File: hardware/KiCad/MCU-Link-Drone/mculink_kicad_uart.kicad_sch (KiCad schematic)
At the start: 11 parts, among them J7 1x3pos, 100mil pitch, U10 SN74LVC1T45GW, U9 SN74LVC1T45GW

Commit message: updated with drone project files
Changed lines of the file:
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@@
 	(text "UART Interface to Target"
 		(exclude_from_sim no)
-		(at 158.75 21.59 0)
+		(at 167.64 21.59 0)
 		(effects
 			(font

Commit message: worked on layout
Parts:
- J7: footprint Connector_PinHeader_2.54mm:PinHeader_1x03_P2.54mm_Horizontal -> Connector_PinHeader_2.54mm:PinHeader_1x03_P2.54mm_Vertical
- U10, U9: footprint Package_TO_SOT_SMD:SOT-23-6 -> Package_TO_SOT_SMD:SOT-363_SC-70-6
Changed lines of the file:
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@@
 			)
 		)
-		(property "Footprint" "Package_TO_SOT_SMD:SOT-23-6"
+		(property "Footprint" "Package_TO_SOT_SMD:SOT-363_SC-70-6"
 			(at 76.2 85.09 0)
 			(effects
@@
 			)
 		)
-		(property "Footprint" "Package_TO_SOT_SMD:SOT-23-6"
+		(property "Footprint" "Package_TO_SOT_SMD:SOT-363_SC-70-6"
 			(at 76.2 123.19 0)
 			(effects
@@
 			)
 		)
-		(property "Footprint" "Connector_PinHeader_2.54mm:PinHeader_1x03_P2.54mm_Horizontal"
+		(property "Footprint" "Connector_PinHeader_2.54mm:PinHeader_1x03_P2.54mm_Vertical"
 			(at 140.97 76.2 0)
 			(effects

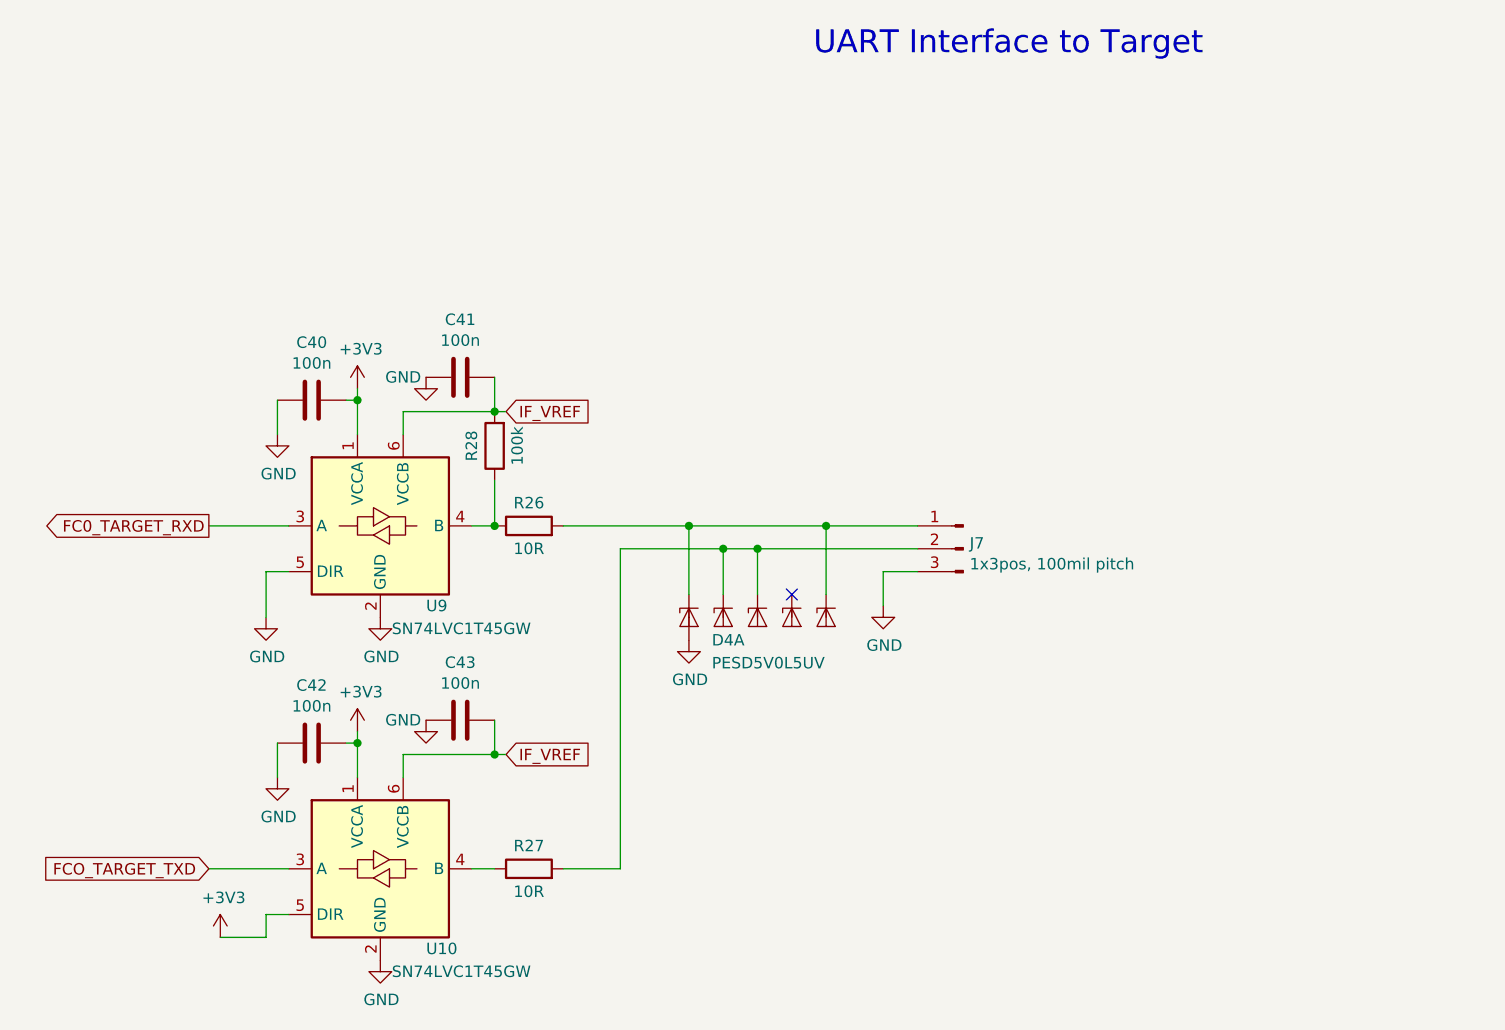
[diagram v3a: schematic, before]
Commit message: added JST-GH for UART
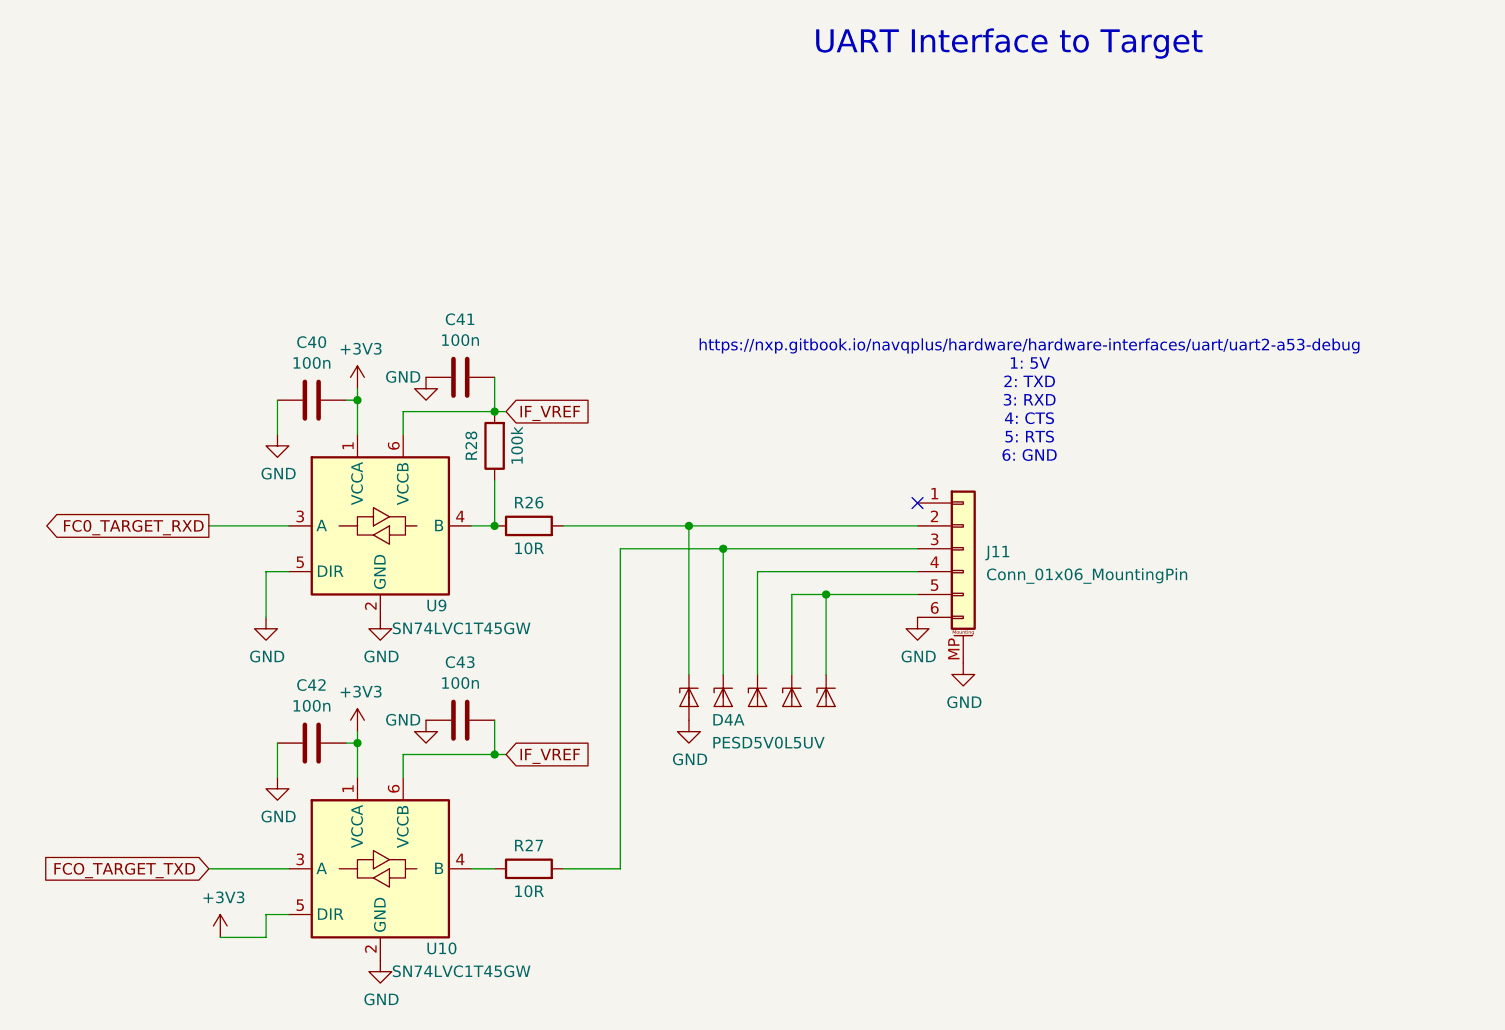
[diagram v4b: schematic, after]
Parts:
- removed J7: 1x3pos, 100mil pitch, Connector_PinHeader_2.54mm:PinHeader_1x03_P2.54mm_Vertical, symbol mculink_kicad-rescue:Conn_01x03_Male-Connector
- added J11: Conn_01x06_MountingPin, Connector_JST:JST_GH_BM06B-GHS-TBT_1x06-1MP_P1.25mm_Vertical, symbol Connector_Generic_MountingPin:Conn_01x06_MountingPin
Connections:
- net GND: now also J11.6 (Pin_6), J11.MP (MountPin)
- net at D4.1 (K1), R26.2: now also J11.2 (Pin_2); no longer D4.6 (K5)
- net at D4.3 (K2), R27.2: now also J11.3 (Pin_3); no longer D4.4 (K3)
- net at D4.5 (K4): now also D4.6 (K5), J11.5 (Pin_5)
- new net: D4.4 (K3), J11.4 (Pin_4)
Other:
- note added: "https://nxp.gitbook.io/navqplus/hardware/hardware-interfaces/uart/uart2-a53-debug 1: 5V 2: TXD 3: RXD 4: CTS 5: RTS 6: GND"
- moved on the sheet: D4A

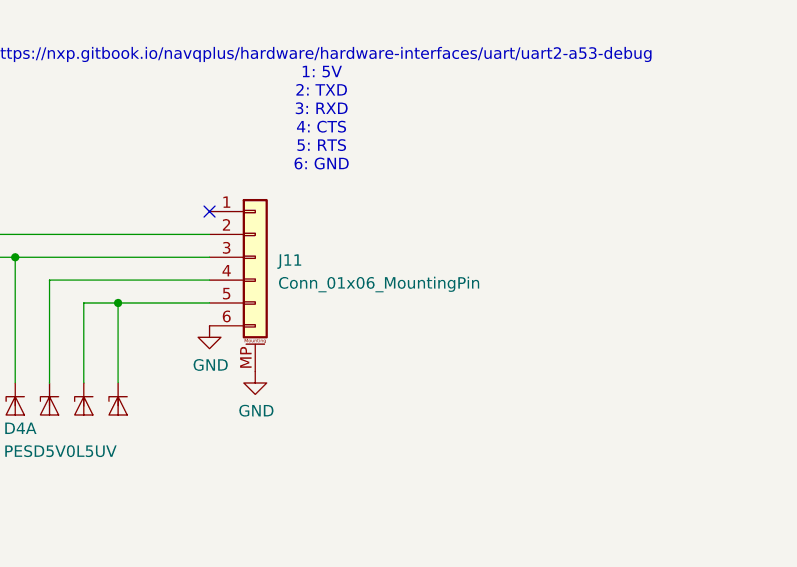
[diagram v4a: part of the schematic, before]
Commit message: updated schematics
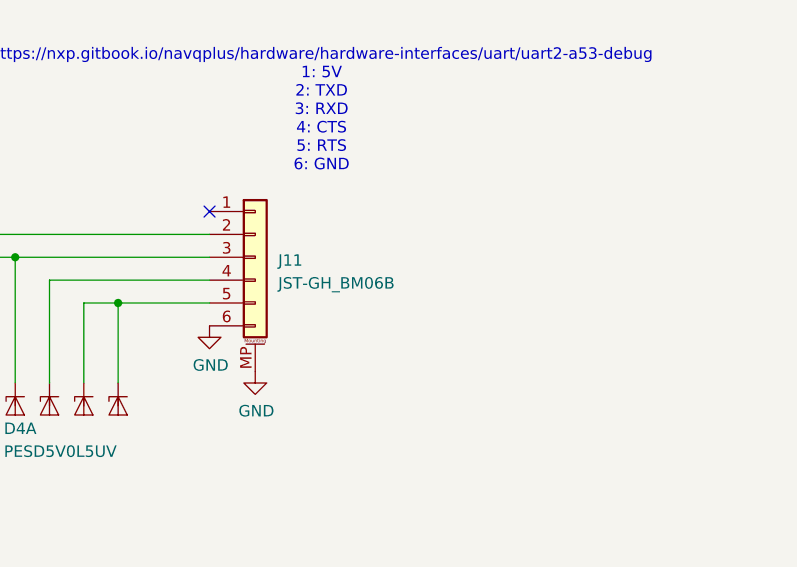
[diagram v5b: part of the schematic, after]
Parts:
- J11: value Conn_01x06_MountingPin -> JST-GH_BM06B
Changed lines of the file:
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@@
 			)
 		)
-		(property "Value" "Conn_01x06_MountingPin"
+		(property "Value" "JST-GH_BM06B"
 			(at 143.51 79.0955 0)
 			(effects

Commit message: updated parts and minor tweaks
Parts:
- J11: distrelec# (none) -> 304-09-562
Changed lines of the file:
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@@
+			)
+		)
+		(property "distrelec#" ""
+			(at 76.2 73.66 0)
+			(effects
+				(font
+					(size 1.27 1.27)
+				)
+				(hide yes)
 			)
 		)
@@
 			)
 		)
+		(property "distrelec#" ""
+			(at 88.9 64.77 0)
+			(effects
+				(font
+					(size 1.27 1.27)
+				)
+				(hide yes)
+			)
+		)
 		(pin "1"
 		)
@@
 			)
 		)
+		(property "distrelec#" ""
+			(at 68.58 59.69 0)
+			(effects
+				(font
+					(size 1.27 1.27)
+				)
+				(hide yes)
+			)
+		)
 		(pin "1"
 		)
@@
 			)
 		)
+		(property "distrelec#" ""
+			(at 85.09 57.15 0)
+			(effects
+				(font
+					(size 1.27 1.27)
+				)
+				(hide yes)
+			)
+		)
 		(pin "1"
 		)
@@
 			)
 		)
+		(property "distrelec#" ""
+			(at 92.71 73.66 0)
+			(effects
+				(font
+					(size 1.27 1.27)
+				)
+				(hide yes)
+			)
+		)
 		(pin "1"
 		)
@@
 			)
 		)
+		(property "distrelec#" ""
+			(at 76.2 111.76 0)
+			(effects
+				(font
+					(size 1.27 1.27)
+				)
+				(hide yes)
+			)
+		)
 		(pin "1"
 		)
@@
 			)
 		)
+		(property "distrelec#" ""
+			(at 68.58 97.79 0)
+			(effects
+				(font
+					(size 1.27 1.27)
+				)
+				(hide yes)
+			)
+		)
 		(pin "1"
 		)
@@
 			)
 		)
+		(property "distrelec#" ""
+			(at 85.09 95.25 0)
+			(effects
+				(font
+					(size 1.27 1.27)
+				)
+				(hide yes)
+			)
+		)
 		(pin "1"
 		)
@@
 			)
 		)
+		(property "distrelec#" ""
+			(at 92.71 111.76 0)
+			(effects
+				(font
+					(size 1.27 1.27)
+				)
+				(hide yes)
+			)
+		)
 		(pin "1"
 		)
@@
 		)
 		(property "Description" "Low capacitance unidirectional fivefold ESD protection diode array, 5.0V, Common Anode, SOT-666"
+			(at 110.49 92.71 0)
+			(effects
+				(font
+					(size 1.27 1.27)
+				)
+				(hide yes)
+			)
+		)
+		(property "distrelec#" ""
 			(at 110.49 92.71 0)
 			(effects
@@
 			)
 		)
+		(property "distrelec#" ""
+			(at 114.3 92.71 0)
+			(effects
+				(font
+					(size 1.27 1.27)
+				)
+				(hide yes)
+			)
+		)
 		(pin "1"
 		)
@@
 			)
 		)
+		(property "distrelec#" ""
+			(at 118.11 92.71 0)
+			(effects
+				(font
+					(size 1.27 1.27)
+				)
+				(hide yes)
+			)
+		)
 		(pin "1"
 		)
@@
 			)
 		)
+		(property "distrelec#" ""
+			(at 121.92 92.71 0)
+			(effects
+				(font
+					(size 1.27 1.27)
+				)
+				(hide yes)
+			)
+		)
 		(pin "1"
 		)
@@
 			)
 		)
+		(property "distrelec#" ""
+			(at 125.73 92.71 0)
+			(effects
+				(font
+					(size 1.27 1.27)
+				)
+				(hide yes)
+			)
+		)
 		(pin "1"
 		)
@@
 			(at 140.97 76.2 0)
 			(effects
+				(font
+					(size 1.27 1.27)
+				)
+				(hide yes)
+			)
+		)
+		(property "distrelec#" "304-09-562"
+			(at 140.97 76.2 0)
+			(effects
